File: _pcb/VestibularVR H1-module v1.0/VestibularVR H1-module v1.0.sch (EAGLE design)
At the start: 67 parts, among them IC1 FT232RL, IC2 74LVC1G07DBV, IC3 LP5907MFX-3.3, IC4 74LVC1G07DBV, IC5 74LVC1G07DBV, IC6 74LVC1G07DBV, IC7 USBLC6-2SC6, IC8 ATXMEGA32A4U, T1 DMG1012UW, T2 DMG1012UW, X1 TSW-105-02-S-D, X15 Main_plug, X2 TSW-105-02-S-D, X3 USB_MINI_B

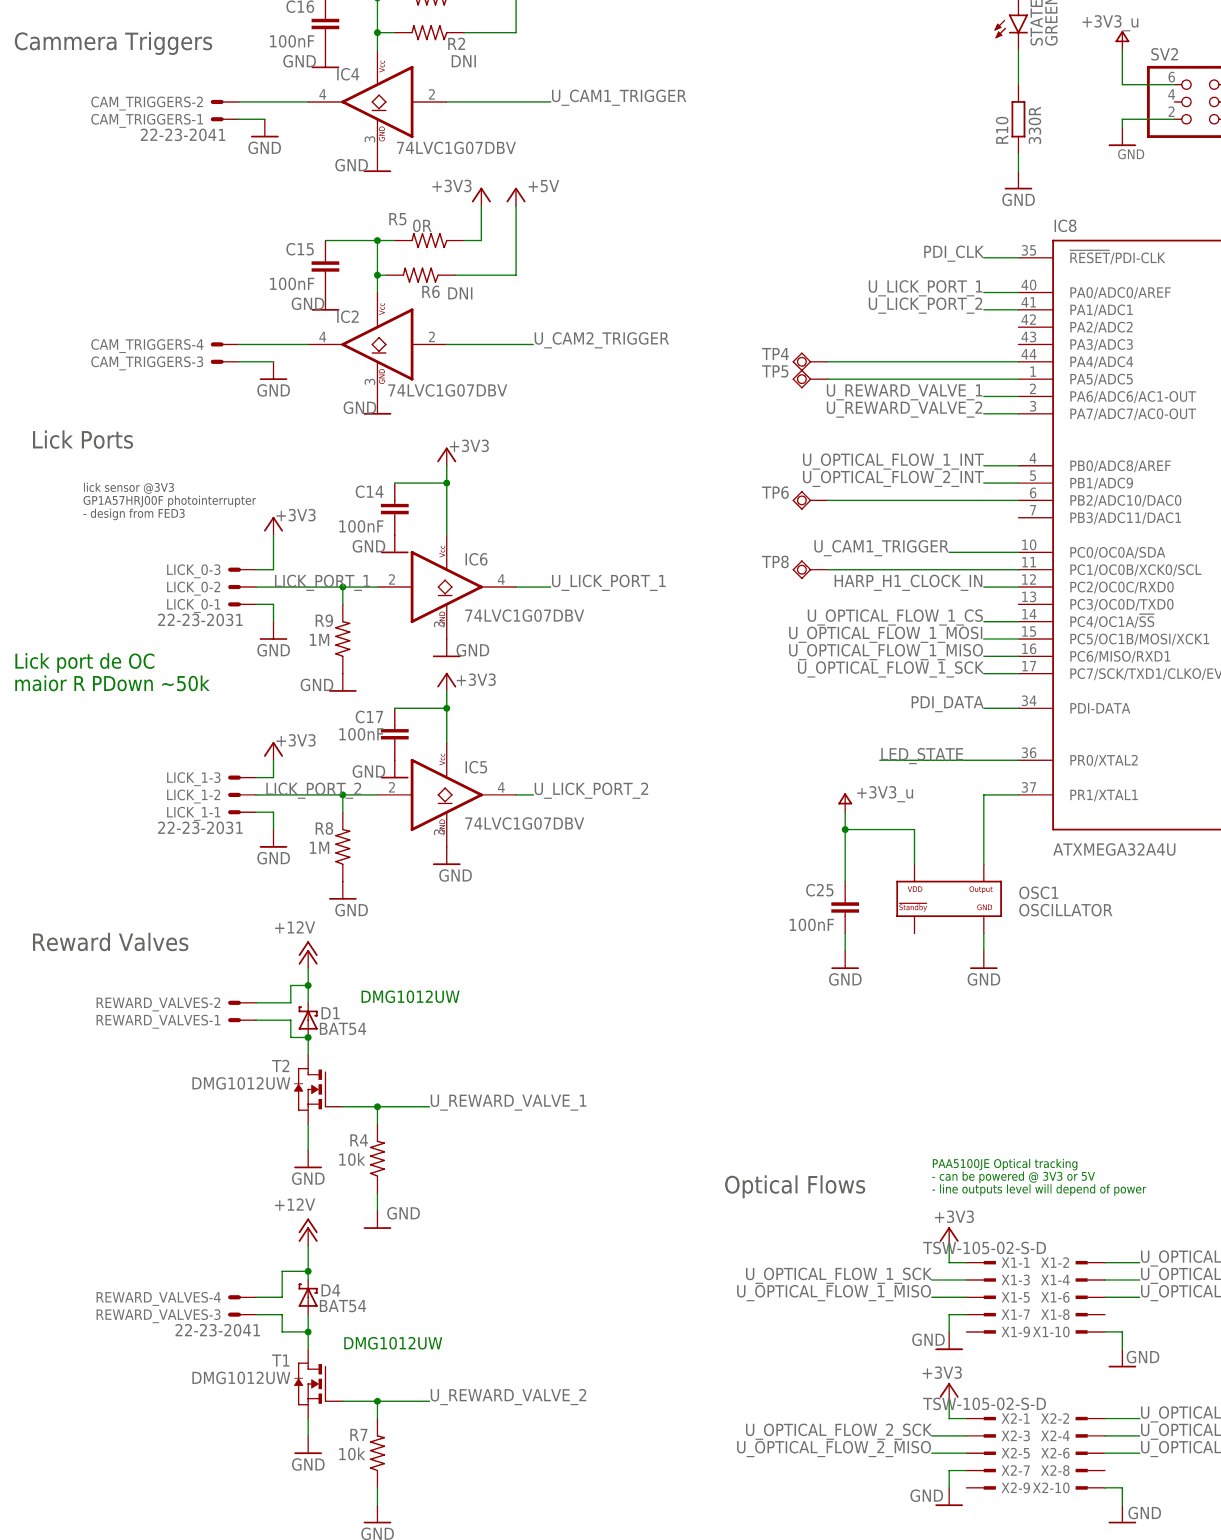
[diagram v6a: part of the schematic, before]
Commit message: BOMs & start Harp Motor device H2-module v1.0
. almost final BOMs versions for VestibularVR H1-module v1.0 & Lick Sensor module v1.0
. start of new project Harp Motor device H2-module v1.0
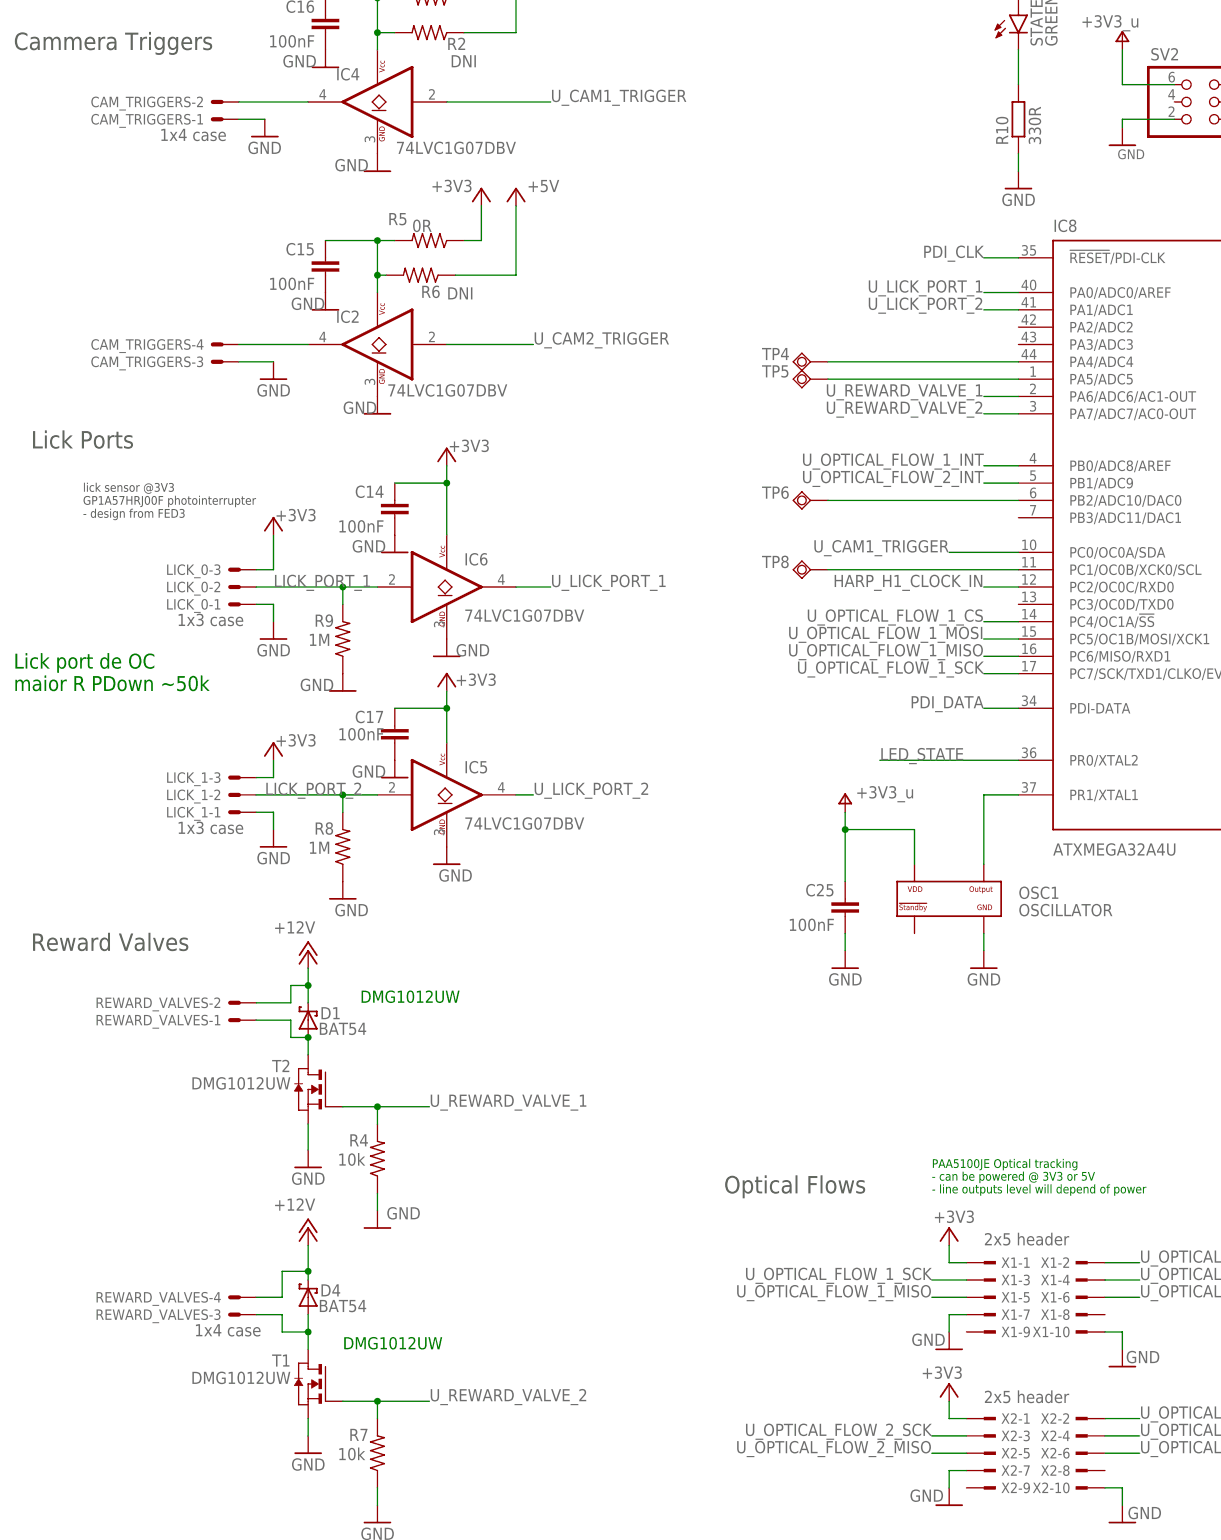
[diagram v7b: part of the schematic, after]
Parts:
- CAM_TRIGGERS, REWARD_VALVES: value 22-23-2041 -> 1x4 case; MF (none) -> -; MPN (none) -> 282834-4 Digikey A98335-ND; OEPS N.A.1 -> OEPS07 xxx1
- IC2, IC4, IC5, IC6: OEPS n.a. -> OEPS08 xxx1
- LICK_0, LICK_1: value 22-23-2031 -> 1x3 case; MF (none) -> -; MPN (none) -> 282834-3 Digikey A98334-ND; OEPS N.A.2 -> OEPS07 xxx2
- X1, X2: value TSW-105-02-S-D -> 2x5 header
- X15: OEPS n.a. -> OEPS07 xxx3

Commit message: VestibularVR H1 module & Lick Sensor module v1.0 FINAL BOMs
final BOM versions
. VestibularVR H1 module
. Lick Sensor module v1.0
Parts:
- CAM_TRIGGERS, REWARD_VALVES: MPN 282834-4 Digikey A98335-ND -> 282834-4; OEPS OEPS07 xxx1 -> OEPS070036
- IC2, IC4, IC5, IC6: MPN SN74LVC1G07DBVR -> M74VHC1GT126DT1G; OEPS OEPS08 xxx1 -> OEPS080017
- LICK_0, LICK_1: MPN 282834-3 Digikey A98334-ND -> 282834-3; OEPS OEPS07 xxx2 -> OEPS070035
- R18, R34: DIGIKEY_PN 541-3959-1-ND -> 541-10.0KLDKR-ND
- R4, R7: DIGIKEY_PN 541-10.0KLCT-ND -> 541-10.0KLDKR-ND
- X15: OEPS OEPS07 xxx3 -> OEPS070037
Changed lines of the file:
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@@
 </part>
 <part name="IC2" library="VestibularVR H1-module v1.0" deviceset="74LVC1G07" device="DBV" package3d_urn="urn:adsk.eagle:package:2406/2">
-<attribute name="MPN" value="SN74LVC1G07DBVR"/>
-<attribute name="OEPS" value="OEPS08 xxx1"/>
+<attribute name="MPN" value="M74VHC1GT126DT1G"/>
+<attribute name="OEPS" value="OEPS080017"/>
 </part>
 <part name="IC4" library="VestibularVR H1-module v1.0" deviceset="74LVC1G07" device="DBV" package3d_urn="urn:adsk.eagle:package:2406/2">
-<attribute name="MPN" value="SN74LVC1G07DBVR"/>
-<attribute name="OEPS" value="OEPS08 xxx1"/>
+<attribute name="MPN" value="M74VHC1GT126DT1G"/>
+<attribute name="OEPS" value="OEPS080017"/>
 </part>
 <part name="IC5" library="VestibularVR H1-module v1.0" deviceset="74LVC1G07" device="DBV" package3d_urn="urn:adsk.eagle:package:2406/2">
-<attribute name="MPN" value="SN74LVC1G07DBVR"/>
-<attribute name="OEPS" value="OEPS08 xxx1"/>
+<attribute name="MPN" value="M74VHC1GT126DT1G"/>
+<attribute name="OEPS" value="OEPS080017"/>
 </part>
 <part name="IC6" library="VestibularVR H1-module v1.0" deviceset="74LVC1G07" device="DBV" package3d_urn="urn:adsk.eagle:package:2406/2">
-<attribute name="MPN" value="SN74LVC1G07DBVR"/>
-<attribute name="OEPS" value="OEPS08 xxx1"/>
+<attribute name="MPN" value="M74VHC1GT126DT1G"/>
+<attribute name="OEPS" value="OEPS080017"/>
 </part>
 <part name="GND65" library="supply1" deviceset="GND" device=""/>
 <part name="R34" library="rcl" library_urn="urn:adsk.eagle:library:334" deviceset="R-US_" device="R0402" package3d_urn="urn:adsk.eagle:package:23547@1/3" value="10k">
-<attribute name="DIGIKEY_PN" value="541-3959-1-ND"/>
+<attribute name="DIGIKEY_PN" value="541-10.0KLDKR-ND"/>
 <attribute name="MPN" value="CRCW040210K0FKED"/>
 <attribute name="OEPS" value="OEPS020030"/>
@@
 <part name="GND3" library="supply1" deviceset="GND" device=""/>
 <part name="R18" library="rcl" library_urn="urn:adsk.eagle:library:334" deviceset="R-US_" device="R0402" package3d_urn="urn:adsk.eagle:package:23547@1/3" value="10k">
-<attribute name="DIGIKEY_PN" value="541-3959-1-ND"/>
+<attribute name="DIGIKEY_PN" value="541-10.0KLDKR-ND"/>
 <attribute name="MPN" value="CRCW040210K0FKED"/>
 <attribute name="OEPS" value="OEPS020030"/>
@@
 </part>
 <part name="R4" library="rcl" library_urn="urn:adsk.eagle:library:334" deviceset="R-US_" device="R0402" package3d_urn="urn:adsk.eagle:package:23547@1/3" value="10k">
-<attribute name="DIGIKEY_PN" value="541-10.0KLCT-ND"/>
+<attribute name="DIGIKEY_PN" value="541-10.0KLDKR-ND"/>
 <attribute name="MPN" value="CRCW040210K0FKED"/>
 <attribute name="OEPS" value="OEPS020030"/>
 </part>
 <part name="R7" library="rcl" library_urn="urn:adsk.eagle:library:334" deviceset="R-US_" device="R0402" package3d_urn="urn:adsk.eagle:package:23547@1/3" value="10k">
-<attribute name="DIGIKEY_PN" value="541-10.0KLCT-ND"/>
+<attribute name="DIGIKEY_PN" value="541-10.0KLDKR-ND"/>
 <attribute name="MPN" value="CRCW040210K0FKED"/>
 <attribute name="OEPS" value="OEPS020030"/>
@@
 <part name="LICK_0" library="con-molex" library_urn="urn:adsk.eagle:library:165" deviceset="22-23-2031" device="" value="1x3 case">
 <attribute name="MF" value="-"/>
-<attribute name="MPN" value="282834-3 Digikey A98334-ND"/>
-<attribute name="OEPS" value="OEPS07 xxx2"/>
+<attribute name="MPN" value="282834-3"/>
+<attribute name="OEPS" value="OEPS070035"/>
 </part>
 <part name="LICK_1" library="con-molex" library_urn="urn:adsk.eagle:library:165" deviceset="22-23-2031" device="" value="1x3 case">
 <attribute name="MF" value="-"/>
-<attribute name="MPN" value="282834-3 Digikey A98334-ND"/>
-<attribute name="OEPS" value="OEPS07 xxx2"/>
+<attribute name="MPN" value="282834-3"/>
+<attribute name="OEPS" value="OEPS070035"/>
 </part>
 <part name="P+6" library="supply1" library_urn="urn:adsk.eagle:library:371" deviceset="+12V" device=""/>
@@
 <part name="CAM_TRIGGERS" library="con-molex" library_urn="urn:adsk.eagle:library:165" deviceset="22-23-2041" device="" value="1x4 case">
 <attribute name="MF" value="-"/>
-<attribute name="MPN" value="282834-4 Digikey A98335-ND"/>
-<attribute name="OEPS" value="OEPS07 xxx1"/>
+<attribute name="MPN" value="282834-4"/>
+<attribute name="OEPS" value="OEPS070036"/>
 </part>
 <part name="X1" library="con-samtec" library_urn="urn:adsk.eagle:library:184" deviceset="TSW-105-02-S-D" device="" value="2x5 header">
@@
 <part name="REWARD_VALVES" library="con-molex" library_urn="urn:adsk.eagle:library:165" deviceset="22-23-2041" device="" value="1x4 case">
 <attribute name="MF" value="-"/>
-<attribute name="MPN" value="282834-4 Digikey A98335-ND"/>
-<attribute name="OEPS" value="OEPS07 xxx1"/>
+<attribute name="MPN" value="282834-4"/>
+<attribute name="OEPS" value="OEPS070036"/>
 </part>
 <part name="X2" library="con-samtec" library_urn="urn:adsk.eagle:library:184" deviceset="TSW-105-02-S-D" device="" value="2x5 header">
@@
 <part name="X15" library="con-weidmueller-sl35" library_urn="urn:adsk.eagle:library:199" deviceset="90G-5" device="" package3d_urn="urn:adsk.eagle:package:11408/1" value="Main_plug">
 <attribute name="MPN" value="20.155MH/5-E"/>
-<attribute name="OEPS" value="OEPS07 xxx3"/>
+<attribute name="OEPS" value="OEPS070037"/>
 </part>
 </parts>
